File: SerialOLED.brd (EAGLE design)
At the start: 27.3 x 27.3 mm, 25 parts, among them IC3 MCP1703CB, U1 ATMEGA328, X1 16 MHz

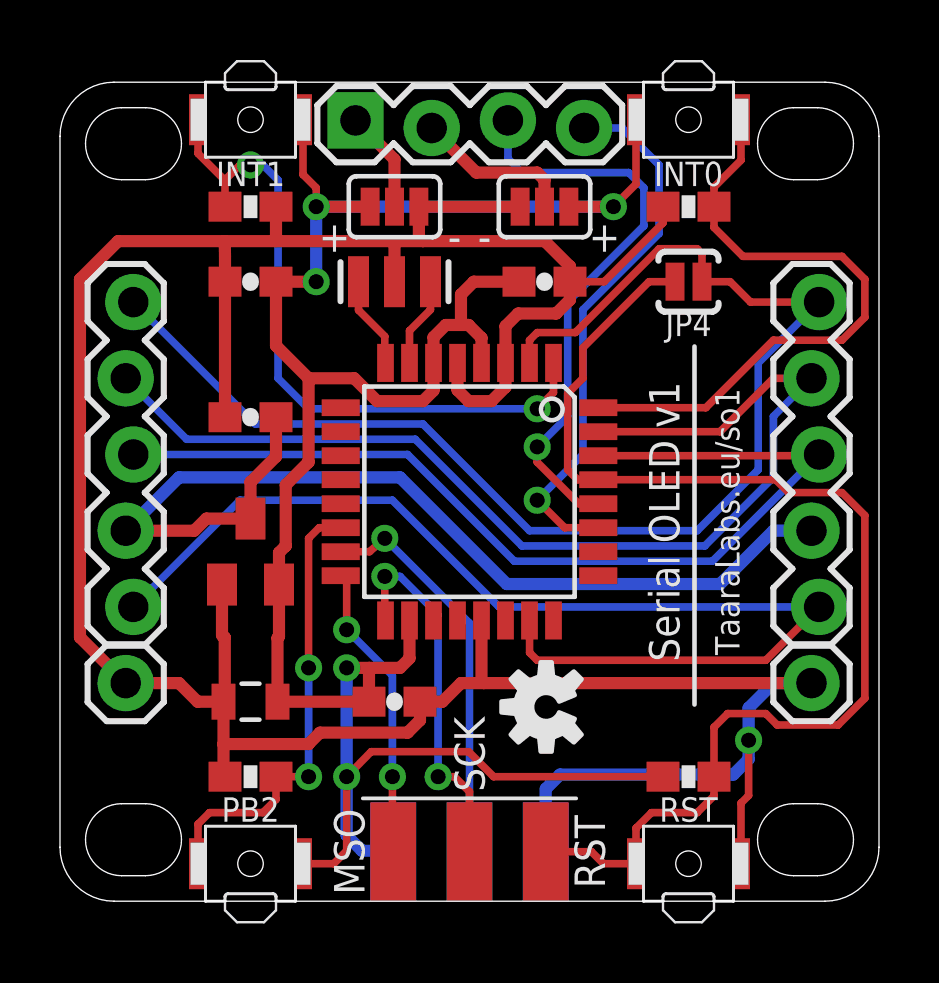
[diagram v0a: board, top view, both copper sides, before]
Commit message: Solder-bridge for FTDI reset replaced with a capacitor
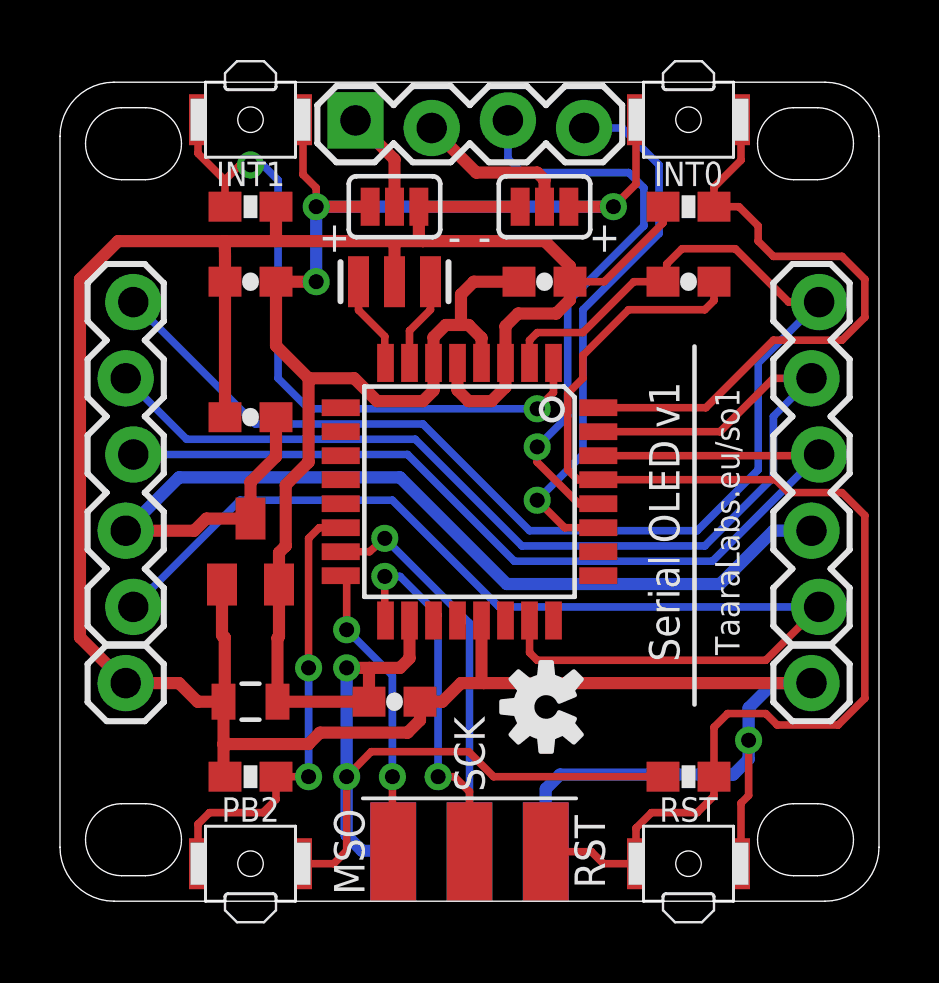
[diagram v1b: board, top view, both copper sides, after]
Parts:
- removed JP4: (no value), SparkFun:SJ_2S-NO
- added C6: 0.1u, SparkFun:0603-CAP
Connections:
- net DTR: now also C6.2; no longer JP4.2
- net RST: now also C6.1; no longer JP4.1
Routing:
- net RST: track 40.3 -> 41.8 mm
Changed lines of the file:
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@@
 <layer number="21" name="tPlace" color="7" fill="1" visible="yes" active="yes"/>
 <layer number="22" name="bPlace" color="7" fill="1" visible="no" active="yes"/>
-<layer number="23" name="tOrigins" color="15" fill="1" visible="no" active="yes"/>
-<layer number="24" name="bOrigins" color="15" fill="1" visible="no" active="yes"/>
+<layer number="23" name="tOrigins" color="15" fill="1" visible="yes" active="yes"/>
+<layer number="24" name="bOrigins" color="15" fill="1" visible="yes" active="yes"/>
 <layer number="25" name="tNames" color="7" fill="1" visible="yes" active="yes"/>
 <layer number="26" name="bNames" color="7" fill="1" visible="no" active="yes"/>
@@
 <element name="U$1" library="SparkFun-Aesthetics" package="OSHW-LOGO-S" value="" x="16.555" y="6.825" rot="R90"/>
 <element name="U$2" library="SparkFun-Aesthetics" package="OSHW-LOGO-S" value="" x="9" y="16" rot="MR90"/>
-<element name="JP4" library="SparkFun" package="SJ_2S-NO" value="" x="21.3" y="21" smashed="yes">
-<attribute name="NAME" x="21.3" y="20" size="0.8128" layer="25" font="vector" ratio="20" align="top-center"/>
-<attribute name="VALUE" x="20.392" y="19.349" size="0.4064" layer="27"/>
+<element name="C6" library="SparkFun" package="0603-CAP" value="0.1u" x="21.3" y="21" smashed="yes" rot="R180">
+<attribute name="VALUE" x="21.3" y="20" size="0.8128" layer="27" font="vector" ratio="20" align="top-center"/>
 </element>
 </elements>
@@
 <wire x1="2.286" y1="22.352" x2="5.842" y2="22.352" width="0.4064" layer="1"/>
 <contactref element="R2" pad="1"/>
-<wire x1="18.492" y1="21" x2="17.35" y2="21" width="0.254" layer="1"/>
 <wire x1="13.096" y1="7" x2="13.716" y2="7.62" width="0.4064" layer="1"/>
 <wire x1="13.716" y1="7.62" x2="14.478" y2="7.62" width="0.4064" layer="1"/>
@@
 <wire x1="20.45" y1="22.958" x2="20.45" y2="23.5" width="0.254" layer="1"/>
 <wire x1="11.5" y1="21" x2="11.5" y2="22.352" width="0.4064" layer="1"/>
+<wire x1="18.492" y1="21" x2="17.35" y2="21" width="0.254" layer="1"/>
 </signal>
 <signal name="MISO">
@@
 <wire x1="27.178" y1="19.812" x2="27.178" y2="21.082" width="0.254" layer="1"/>
 <wire x1="27.178" y1="21.082" x2="26.416" y2="21.844" width="0.254" layer="1"/>
-<wire x1="26.416" y1="21.844" x2="23.114" y2="21.844" width="0.254" layer="1"/>
-<wire x1="23.114" y1="21.844" x2="22.15" y2="22.808" width="0.254" layer="1"/>
 <wire x1="22.352" y1="23.366" x2="22.15" y2="23.5" width="0.254" layer="1"/>
 <wire x1="23.05" y1="26.4" x2="23.05" y2="25.05" width="0.254" layer="1"/>
 <wire x1="23.05" y1="25.05" x2="22.15" y2="24.15" width="0.254" layer="1"/>
 <wire x1="22.15" y1="24.15" x2="22.15" y2="23.5" width="0.254" layer="1"/>
-<wire x1="22.15" y1="22.808" x2="22.15" y2="23.5" width="0.254" layer="1"/>
+<wire x1="26.416" y1="21.844" x2="24.13" y2="21.844" width="0.254" layer="1"/>
+<wire x1="24.13" y1="21.844" x2="23.622" y2="22.352" width="0.254" layer="1"/>
+<wire x1="23.622" y1="22.352" x2="23.622" y2="22.86" width="0.254" layer="1"/>
+<wire x1="23.622" y1="22.86" x2="22.982" y2="23.5" width="0.254" layer="1"/>
+<wire x1="22.982" y1="23.5" x2="22.15" y2="23.5" width="0.254" layer="1"/>
 </signal>
 <signal name="D7">
@@
 <wire x1="21.59" y1="3.302" x2="22.15" y2="3.862" width="0.254" layer="1"/>
 <wire x1="22.15" y1="3.862" x2="22.15" y2="4.5" width="0.254" layer="1"/>
-<contactref element="JP4" pad="1"/>
-<wire x1="20.85" y1="21" x2="19.984" y2="21" width="0.254" layer="1"/>
-<wire x1="19.984" y1="21" x2="17.78" y2="18.796" width="0.254" layer="1"/>
-<wire x1="17.78" y1="18.796" x2="17.78" y2="17.78" width="0.254" layer="1"/>
+<wire x1="17.78" y1="18.542" x2="17.78" y2="17.78" width="0.254" layer="1"/>
 <wire x1="17.78" y1="17.78" x2="17.272" y2="17.272" width="0.254" layer="1"/>
 <wire x1="17.272" y1="17.272" x2="17.272" y2="14.732" width="0.254" layer="1"/>
 <wire x1="17.272" y1="14.732" x2="17.604" y2="14.4" width="0.254" layer="1"/>
 <wire x1="17.604" y1="14.4" x2="18.2926" y2="14.4" width="0.254" layer="1"/>
+<contactref element="C6" pad="1"/>
+<wire x1="22.15" y1="21" x2="22.15" y2="20.372" width="0.254" layer="1"/>
+<wire x1="22.15" y1="20.372" x2="21.844" y2="20.066" width="0.254" layer="1"/>
+<wire x1="21.844" y1="20.066" x2="19.304" y2="20.066" width="0.254" layer="1"/>
+<wire x1="19.304" y1="20.066" x2="17.78" y2="18.542" width="0.254" layer="1"/>
 </signal>
 <signal name="N$1">
@@
 <wire x1="16" y1="18.2926" x2="16" y2="19.048" width="0.254" layer="1"/>
 <wire x1="16" y1="19.048" x2="16.256" y2="19.304" width="0.254" layer="1"/>
-<wire x1="23.368" y1="20.32" x2="25.654" y2="20.32" width="0.254" layer="1"/>
+<wire x1="23.368" y1="20.32" x2="25.654" y2="20.32" width="0" layer="19" extent="1-16"/>
 <wire x1="2.794" y1="20.32" x2="6.858" y2="16.256" width="0.254" layer="16"/>
 <wire x1="6.858" y1="16.256" x2="12.446" y2="16.256" width="0.254" layer="16"/>
@@
 <wire x1="23.622" y1="14.732" x2="23.622" y2="18.288" width="0.254" layer="16"/>
 <wire x1="23.622" y1="18.288" x2="25.654" y2="20.32" width="0.254" layer="16"/>
-<contactref element="JP4" pad="2"/>
-<wire x1="16.256" y1="19.304" x2="17.526" y2="19.304" width="0.254" layer="1"/>
-<wire x1="17.526" y1="19.304" x2="20.32" y2="22.098" width="0.254" layer="1"/>
-<wire x1="20.32" y1="22.098" x2="21.59" y2="22.098" width="0.254" layer="1"/>
-<wire x1="21.59" y1="22.098" x2="21.75" y2="21.938" width="0.254" layer="1"/>
-<wire x1="21.75" y1="21.938" x2="21.75" y2="21" width="0.254" layer="1"/>
-<wire x1="21.75" y1="21" x2="22.688" y2="21" width="0.254" layer="1"/>
-<wire x1="22.688" y1="21" x2="23.368" y2="20.32" width="0.254" layer="1"/>
+<wire x1="16.256" y1="19.304" x2="17.78" y2="19.304" width="0.254" layer="1"/>
+<contactref element="C6" pad="2"/>
+<wire x1="17.78" y1="19.304" x2="19.476" y2="21" width="0.254" layer="1"/>
+<wire x1="19.476" y1="21" x2="20.45" y2="21" width="0.254" layer="1"/>
+<wire x1="20.45" y1="21" x2="20.574" y2="21.124" width="0.254" layer="1"/>
+<wire x1="20.574" y1="21.124" x2="20.574" y2="21.59" width="0.254" layer="1"/>
+<wire x1="20.574" y1="21.59" x2="21.082" y2="22.098" width="0.254" layer="1"/>
+<wire x1="21.082" y1="22.098" x2="22.86" y2="22.098" width="0.254" layer="1"/>
+<wire x1="22.86" y1="22.098" x2="24.638" y2="20.32" width="0.254" layer="1"/>
+<wire x1="24.638" y1="20.32" x2="25.654" y2="20.32" width="0.254" layer="1"/>
 </signal>
 <signal name="A1">

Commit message: Board fixes and new pictures
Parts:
- turned U$6 to 180 degrees
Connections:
- net RXD: now also JP3.5; no longer JP3.4
- net TXD: now also JP3.4; no longer JP3.5
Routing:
- net RXD: track 33.2 -> 45.9 mm
- net 3.3V: track 81.0 -> 90.8 mm, vias 5 -> 6
- net RST: track 41.8 -> 51.3 mm
- net MISO: track 9.93 -> 15.0 mm
- net GND: track 107.8 -> 111.3 mm
- net TXD: track 36.5 -> 35.0 mm
- net MOSI: track 13.3 -> 14.1 mm
- net CTS: track 37.4 -> 37.9 mm
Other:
- board text added: "<RX"
- board text added: "TX>"
